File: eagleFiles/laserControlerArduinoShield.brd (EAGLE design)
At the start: 53 x 59.7 mm, 2 parts, among them T1 74990110013

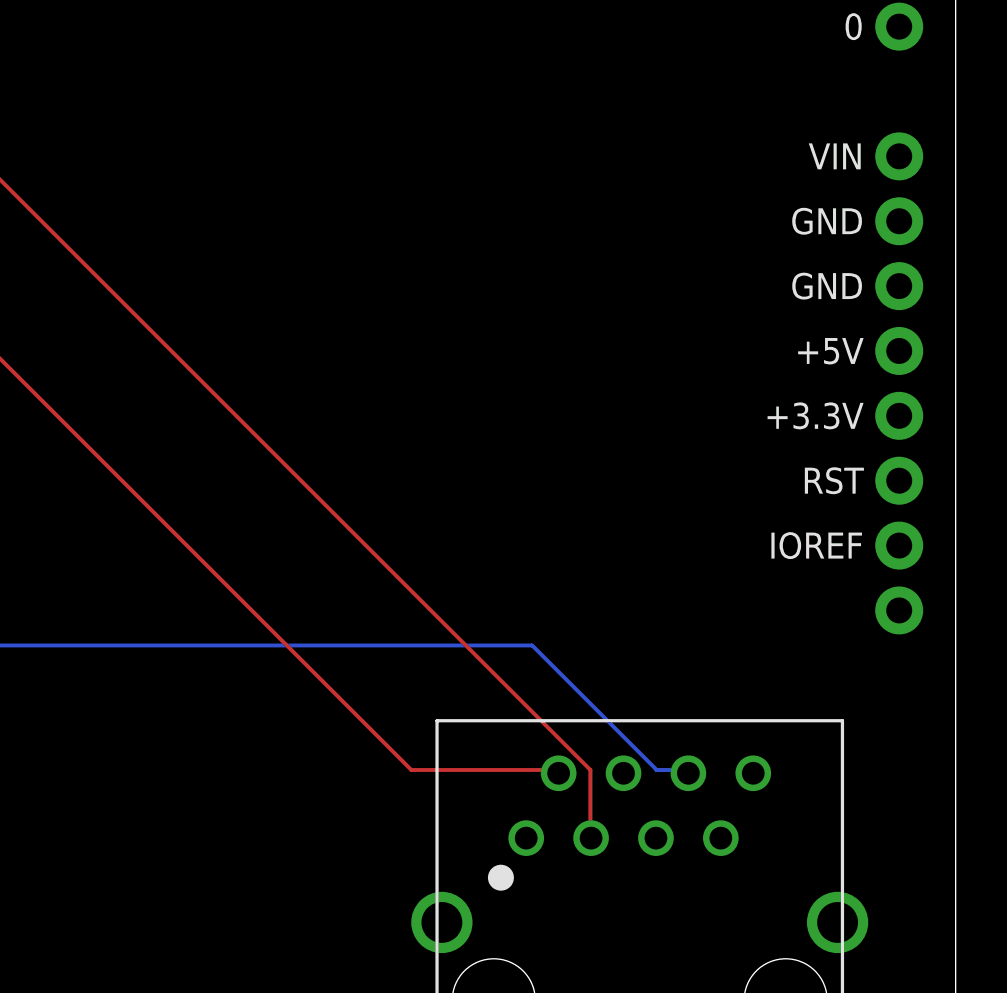
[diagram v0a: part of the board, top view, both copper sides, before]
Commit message: connect pins 4-5 in ethernet connector to turn the laser on
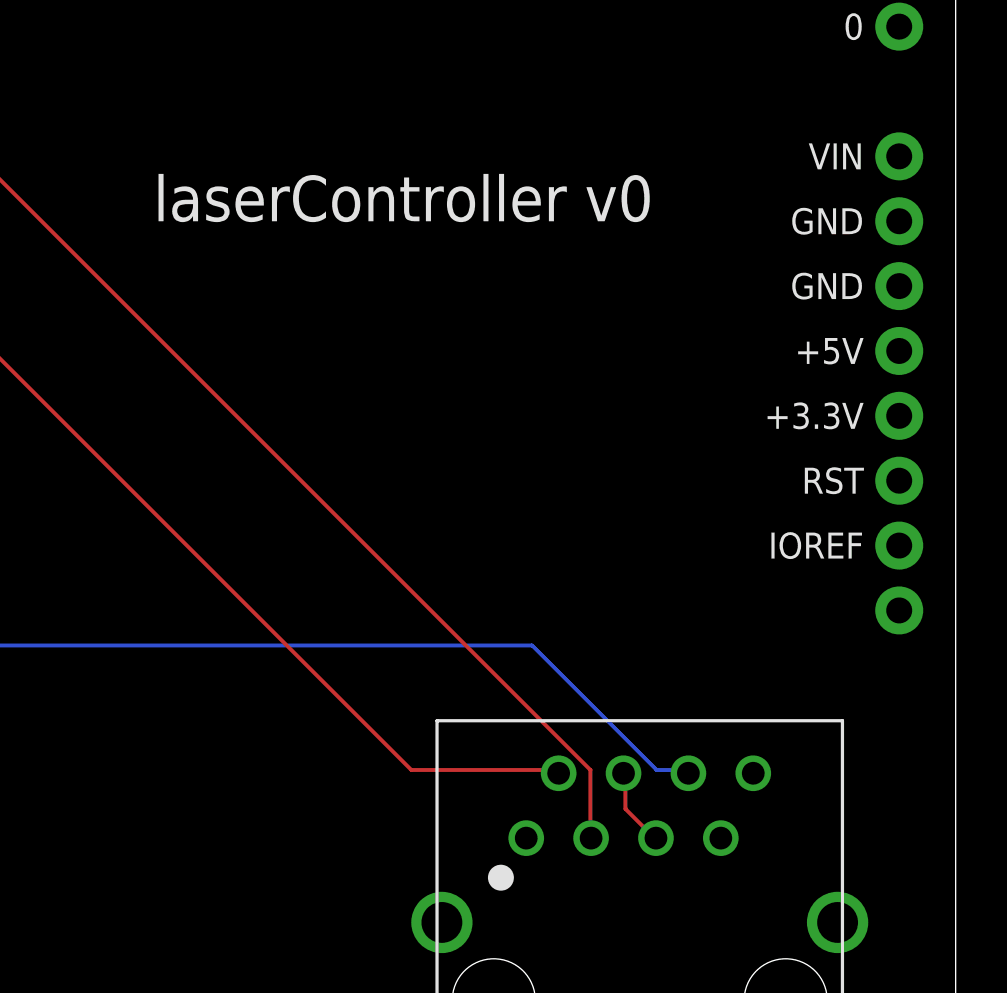
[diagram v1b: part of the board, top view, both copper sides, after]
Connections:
- new net N$3: T1.4, T1.5
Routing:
- net N$3: track 0.00 -> 3.11 mm
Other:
- board text added: "laserController v0"
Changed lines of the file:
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@@
 <wire x1="53.01" y1="59.68" x2="0" y2="59.68" width="0" layer="20"/>
 <wire x1="0" y1="59.68" x2="0" y2="0" width="0" layer="20"/>
+<text x="21.59" y="34.29" size="1.778" layer="25">laserController v0</text>
 </plain>
 <attributes>
@@
 <wire x1="2.5908" y1="46.9392" x2="2.54" y2="46.99" width="0.1524" layer="1"/>
 </signal>
+<signal name="N$3">
+<contactref element="T1" pad="4"/>
+<contactref element="T1" pad="5"/>
+<wire x1="40.0812" y1="11.2776" x2="40.0812" y2="12.6492" width="0.1524" layer="1"/>
+<wire x1="41.148" y1="10.2108" x2="40.0812" y2="11.2776" width="0.1524" layer="1"/>
+<wire x1="40.0812" y1="12.6492" x2="40.005" y2="12.6746" width="0.1524" layer="1"/>
+<wire x1="41.148" y1="10.2108" x2="41.275" y2="10.1346" width="0.1524" layer="1"/>
+</signal>
 </signals>

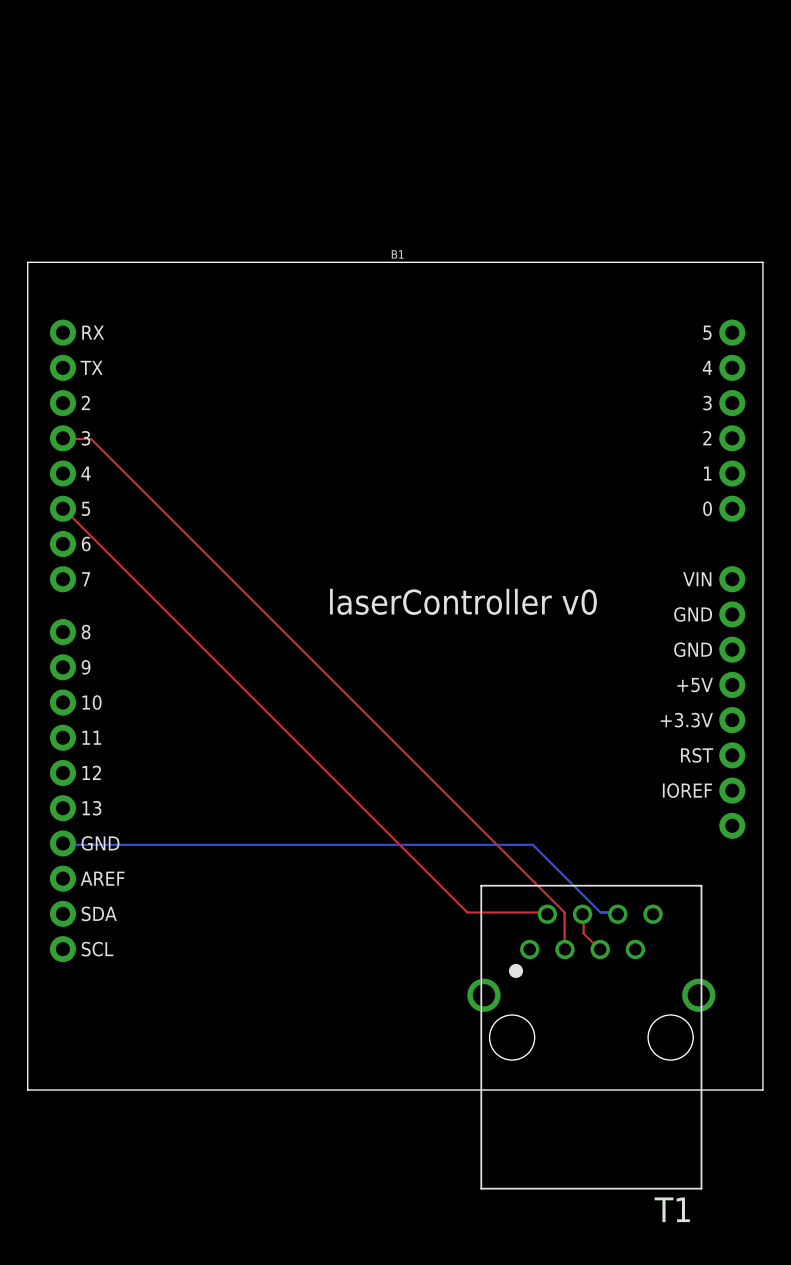
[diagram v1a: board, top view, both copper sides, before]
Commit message: add bnc connectors to arduino shield to sent ttl to recording system
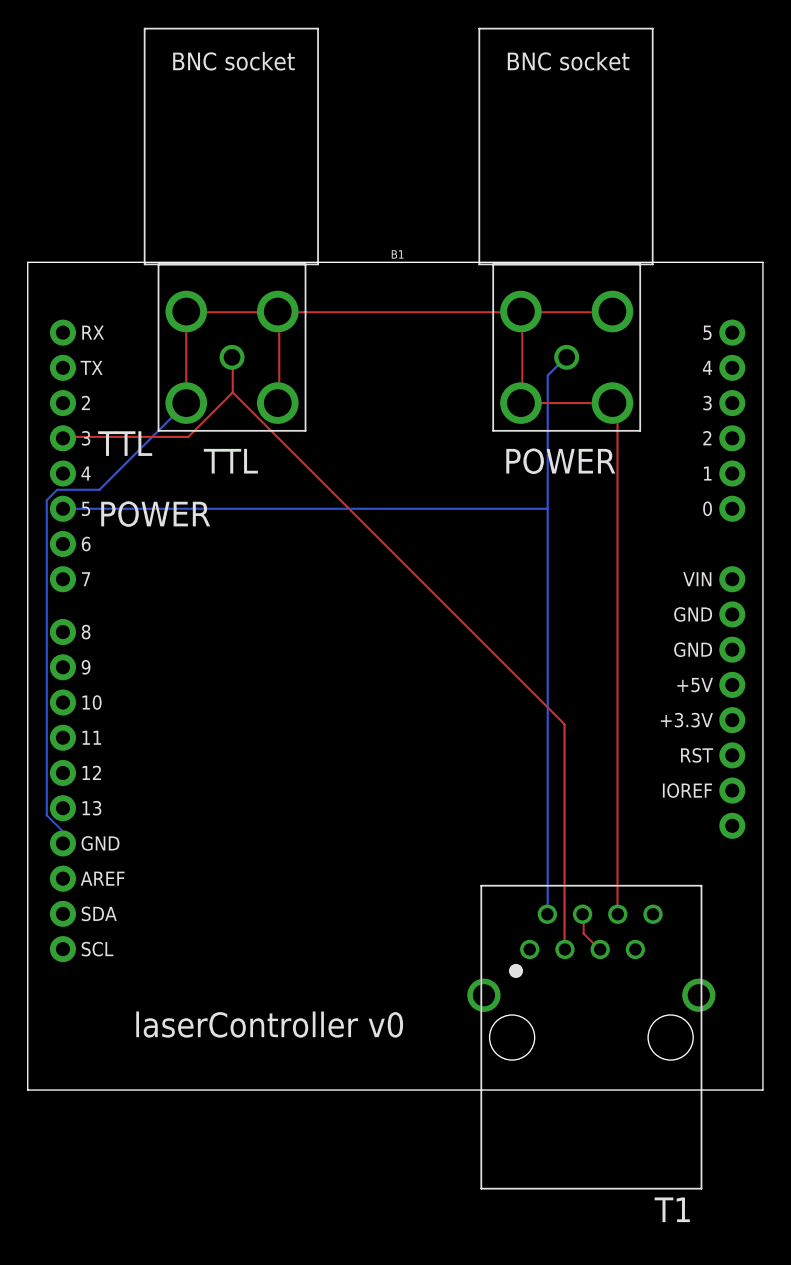
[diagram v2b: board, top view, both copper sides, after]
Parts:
- added BNC_POWER, BNC_TTL: BNC_SOCKET, My_library:BNC_SOCKET
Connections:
- net DGND: now also BNC_POWER.P$1, BNC_POWER.P$2, BNC_POWER.P$3, BNC_POWER.P$4, BNC_TTL.P$1, BNC_TTL.P$2, BNC_TTL.P$3, BNC_TTL.P$4
- net N$1: now also BNC_TTL.P$SIGNAL
- net N$2: now also BNC_POWER.P$SIGNAL
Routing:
- net DGND: track 42.2 -> 132.5 mm
- net N$1: track 47.0 -> 75.7 mm
- net N$2: track 53.0 -> 66.3 mm
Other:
- board text added: "POWER"
- board text added: "TTL"
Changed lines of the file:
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@@
 <wire x1="53.01" y1="59.68" x2="0" y2="59.68" width="0" layer="20"/>
 <wire x1="0" y1="59.68" x2="0" y2="0" width="0" layer="20"/>
-<text x="21.59" y="34.29" size="1.778" layer="25">laserController v0</text>
+<text x="7.62" y="3.81" size="1.778" layer="25">laserController v0</text>
+<text x="12.7" y="44.45" size="1.778" layer="25">TTL</text>
+<text x="34.29" y="44.45" size="1.778" layer="25">POWER</text>
+<text x="5.08" y="45.72" size="1.778" layer="25">TTL</text>
+<text x="5.08" y="40.64" size="1.778" layer="25">POWER</text>
 </plain>
 <attributes>
@@
 <attribute name="VALUE" x="47.6631" y="16.9926" size="1.27" layer="27" rot="R180"/>
 </element>
+<element name="BNC_TTL" library="My_library" package="BNC_SOCKET" value="BNC_SOCKET" x="35.56" y="49.53" smashed="yes"/>
+<element name="BNC_POWER" library="My_library" package="BNC_SOCKET" value="BNC_SOCKET" x="11.43" y="49.53" smashed="yes"/>
 </elements>
 <signals>
@@
 <contactref element="B1" pad="GND@2"/>
 <contactref element="T1" pad="6"/>
-<wire x1="41.3004" y1="12.8016" x2="42.5196" y2="12.8016" width="0.1524" layer="16"/>
-<wire x1="36.4236" y1="17.6784" x2="41.3004" y2="12.8016" width="0.1524" layer="16"/>
-<wire x1="2.5908" y1="17.6784" x2="36.4236" y2="17.6784" width="0.1524" layer="16"/>
-<wire x1="42.5196" y1="12.8016" x2="42.545" y2="12.6746" width="0.1524" layer="16"/>
-<wire x1="2.5908" y1="17.6784" x2="2.54" y2="17.78" width="0.1524" layer="16"/>
+<contactref element="BNC_TTL" pad="P$2"/>
+<contactref element="BNC_TTL" pad="P$1"/>
+<contactref element="BNC_TTL" pad="P$4"/>
+<contactref element="BNC_TTL" pad="P$3"/>
+<contactref element="BNC_POWER" pad="P$2"/>
+<contactref element="BNC_POWER" pad="P$1"/>
+<contactref element="BNC_POWER" pad="P$4"/>
+<contactref element="BNC_POWER" pad="P$3"/>
+<wire x1="42.0624" y1="56.0832" x2="35.6616" y2="56.0832" width="0.1524" layer="1"/>
+<wire x1="42.0624" y1="56.0832" x2="42.16" y2="56.13" width="0.1524" layer="1"/>
+<wire x1="42.5196" y1="49.2252" x2="42.5196" y2="12.8016" width="0.1524" layer="1"/>
+<wire x1="42.2148" y1="49.53" x2="42.5196" y2="49.2252" width="0.1524" layer="1"/>
+<wire x1="42.5196" y1="12.8016" x2="42.545" y2="12.6746" width="0.1524" layer="1"/>
+<wire x1="42.2148" y1="49.53" x2="42.16" y2="49.53" width="0.1524" layer="1"/>
+<wire x1="42.16" y1="49.53" x2="35.6616" y2="49.53" width="0.1524" layer="1"/>
+<wire x1="35.6616" y1="49.53" x2="35.6616" y2="56.0832" width="0.1524" layer="1"/>
+<wire x1="35.6616" y1="56.0832" x2="35.56" y2="56.13" width="0.1524" layer="1"/>
+<wire x1="35.6616" y1="49.53" x2="35.56" y2="49.53" width="0.1524" layer="1"/>
+<wire x1="18.1356" y1="56.0832" x2="18.1356" y2="49.53" width="0.1524" layer="1"/>
+<wire x1="18.1356" y1="49.53" x2="18.03" y2="49.53" width="0.1524" layer="1"/>
+<wire x1="17.9832" y1="56.0832" x2="11.43" y2="56.0832" width="0.1524" layer="1"/>
+<wire x1="17.9832" y1="56.0832" x2="18.03" y2="56.13" width="0.1524" layer="1"/>
+<wire x1="2.4384" y1="18.7452" x2="2.4384" y2="17.8308" width="0.1524" layer="16"/>
+<wire x1="1.3716" y1="19.812" x2="2.4384" y2="18.7452" width="0.1524" layer="16"/>
+<wire x1="1.3716" y1="42.5196" x2="1.3716" y2="19.812" width="0.1524" layer="16"/>
+<wire x1="2.1336" y1="43.2816" x2="1.3716" y2="42.5196" width="0.1524" layer="16"/>
+<wire x1="5.1816" y1="43.2816" x2="2.1336" y2="43.2816" width="0.1524" layer="16"/>
+<wire x1="11.43" y1="49.53" x2="5.1816" y2="43.2816" width="0.1524" layer="16"/>
+<wire x1="2.4384" y1="17.8308" x2="2.54" y2="17.78" width="0.1524" layer="16"/>
+<wire x1="11.43" y1="49.53" x2="11.43" y2="56.0832" width="0.1524" layer="1"/>
+<wire x1="11.43" y1="56.0832" x2="11.43" y2="56.13" width="0.1524" layer="1"/>
+<wire x1="18.1356" y1="56.0832" x2="35.5092" y2="56.0832" width="0.1524" layer="1"/>
+<wire x1="35.5092" y1="56.0832" x2="35.56" y2="56.13" width="0.1524" layer="1"/>
+<wire x1="18.1356" y1="56.0832" x2="18.03" y2="56.13" width="0.1524" layer="1"/>
 </signal>
 <signal name="N$1">
 <contactref element="B1" pad="D5"/>
 <contactref element="T1" pad="2"/>
-<wire x1="31.6992" y1="12.8016" x2="37.338" y2="12.8016" width="0.1524" layer="1"/>
-<wire x1="2.5908" y1="41.91" x2="31.6992" y2="12.8016" width="0.1524" layer="1"/>
-<wire x1="37.338" y1="12.8016" x2="37.465" y2="12.6746" width="0.1524" layer="1"/>
-<wire x1="2.5908" y1="41.91" x2="2.54" y2="41.91" width="0.1524" layer="1"/>
+<contactref element="BNC_TTL" pad="P$SIGNAL"/>
+<wire x1="37.4904" y1="51.5112" x2="37.4904" y2="41.91" width="0.1524" layer="16"/>
+<wire x1="37.4904" y1="41.91" x2="37.4904" y2="12.8016" width="0.1524" layer="16"/>
+<wire x1="38.7096" y1="52.7304" x2="37.4904" y2="51.5112" width="0.1524" layer="16"/>
+<wire x1="37.4904" y1="12.8016" x2="37.465" y2="12.6746" width="0.1524" layer="16"/>
+<wire x1="38.7096" y1="52.7304" x2="38.86" y2="52.83" width="0.1524" layer="16"/>
+<wire x1="37.4904" y1="41.91" x2="2.54" y2="41.91" width="0.1524" layer="16"/>
 </signal>
 <signal name="N$2">
 <contactref element="B1" pad="D3"/>
 <contactref element="T1" pad="3"/>
-<wire x1="38.7096" y1="12.8016" x2="38.7096" y2="10.2108" width="0.1524" layer="1"/>
-<wire x1="4.572" y1="46.9392" x2="38.7096" y2="12.8016" width="0.1524" layer="1"/>
-<wire x1="2.5908" y1="46.9392" x2="4.572" y2="46.9392" width="0.1524" layer="1"/>
+<contactref element="BNC_POWER" pad="P$SIGNAL"/>
+<wire x1="38.7096" y1="26.3652" x2="38.7096" y2="10.2108" width="0.1524" layer="1"/>
+<wire x1="14.7828" y1="50.292" x2="38.7096" y2="26.3652" width="0.1524" layer="1"/>
+<wire x1="14.7828" y1="52.7304" x2="14.7828" y2="50.292" width="0.1524" layer="1"/>
 <wire x1="38.7096" y1="10.2108" x2="38.735" y2="10.1346" width="0.1524" layer="1"/>
-<wire x1="2.5908" y1="46.9392" x2="2.54" y2="46.99" width="0.1524" layer="1"/>
+<wire x1="14.7828" y1="52.7304" x2="14.73" y2="52.83" width="0.1524" layer="1"/>
+<wire x1="11.5824" y1="47.0916" x2="2.5908" y2="47.0916" width="0.1524" layer="1"/>
+<wire x1="14.7828" y1="50.292" x2="11.5824" y2="47.0916" width="0.1524" layer="1"/>
+<wire x1="2.5908" y1="47.0916" x2="2.54" y2="46.99" width="0.1524" layer="1"/>
 </signal>
 <signal name="N$3">
